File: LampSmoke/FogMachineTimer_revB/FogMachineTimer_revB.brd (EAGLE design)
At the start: 160 x 100 mm, 5 parts, among them IC1 ATTINY85-20SU, J1 M20-9980346, J2 CUI_PJ-037ACUI_PJ-037A_0_0, U1 LH1540AABTR

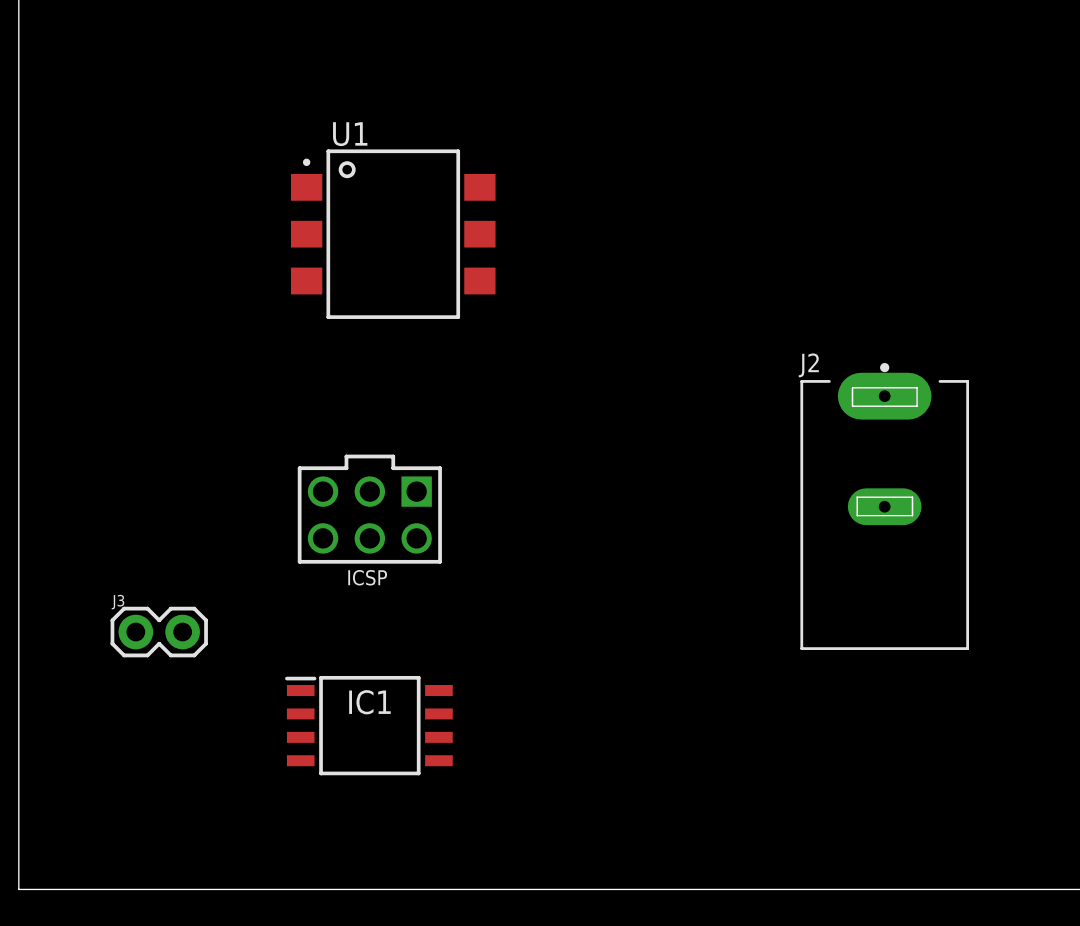
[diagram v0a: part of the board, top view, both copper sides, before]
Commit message: corrected polarity
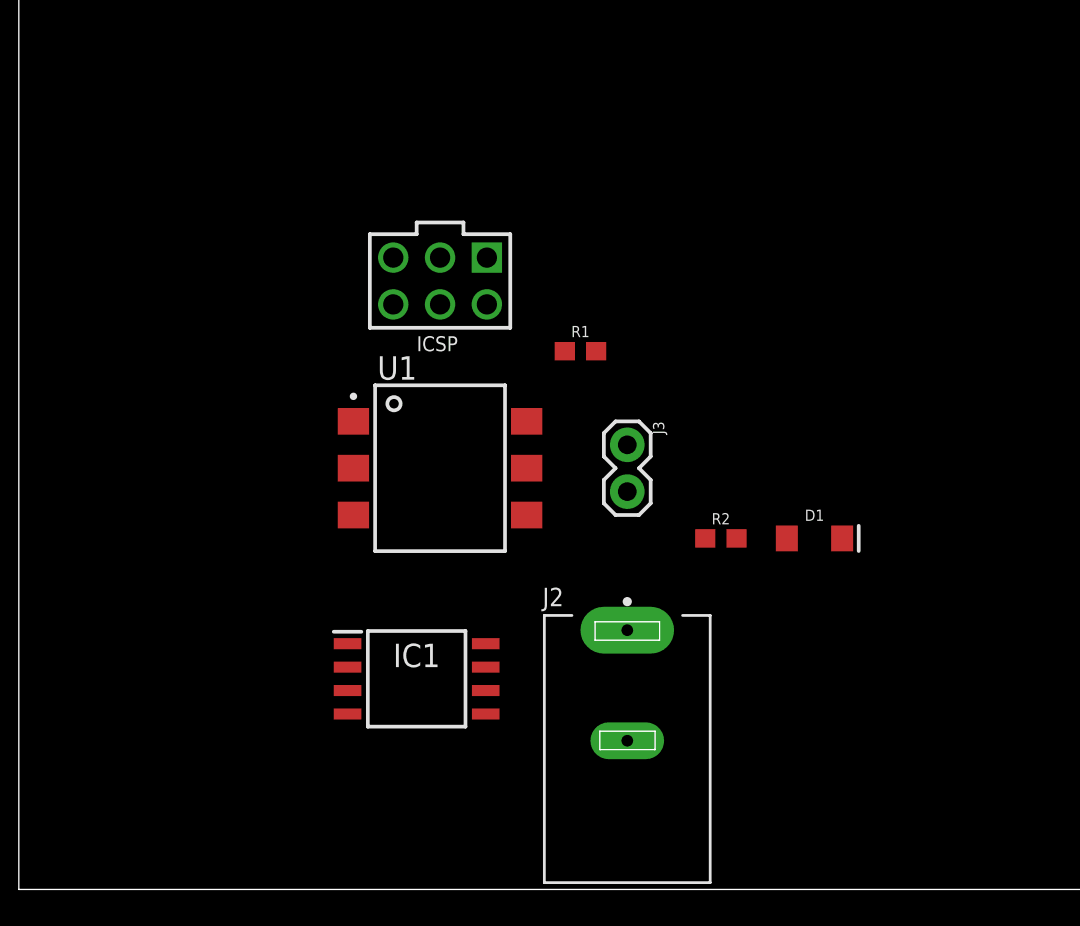
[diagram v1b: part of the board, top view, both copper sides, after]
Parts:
- added D1: (no value), SparkFun-LED:LED-1206
- added R1: 1k, SparkFun-Resistors:0603
- added R2: 220R, SparkFun-Resistors:0603
- moved J3 28.5 mm to (33.0, 24.1), turned to 270 degrees
- moved J2 18.9 mm to (33.0, 7.62)
- moved J1 13.3 mm to (22.9, 30.5)
- moved U1 13.0 mm to (22.9, 22.9)
- moved IC1 3.59 mm to (21.6, 11.4)
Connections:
- new net N$1: D1.A, R2.1
- new net U1_P6: R1.1, U1.6
- net GND: now also D1.C, U1.2; no longer U1.1
- net PB0: now also U1.1; no longer U1.2
- net PB1: now also R2.2
- net SW_POS: now also R1.2; no longer U1.6

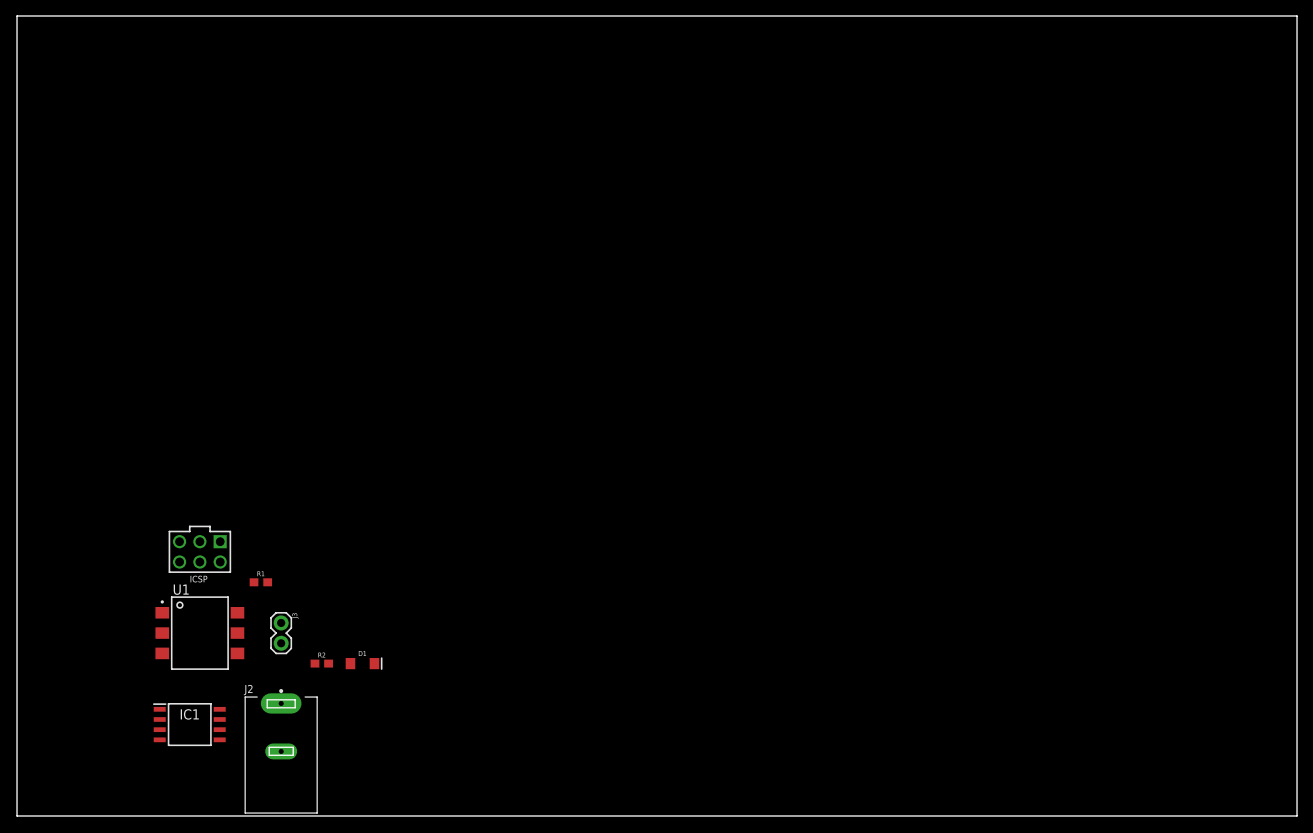
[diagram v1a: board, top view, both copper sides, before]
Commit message: FogMachineTimer revB submitted to OSHPark
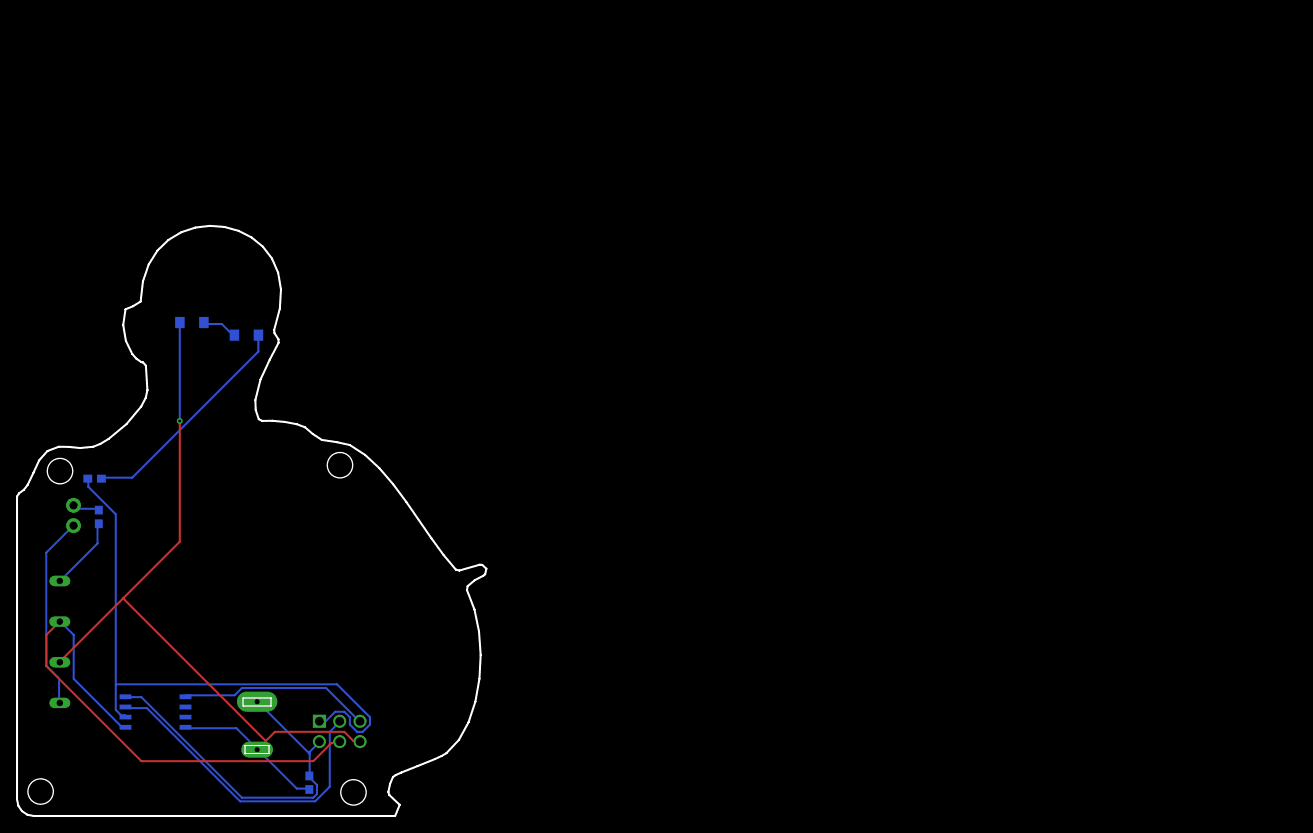
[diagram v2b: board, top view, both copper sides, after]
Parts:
- removed IC1: ATTINY85-20SU, NickParts:SOT127P798X216-8N
- removed U1: LH1540AABTR, NickParts:SOIC254P1005X390-6N
- added ATTINY85: ATTINY85-20SU, NickParts:SOT127P798X216-8N
- added C1: 0.1uF, SparkFun-Capacitors:0603
- added D2: (no value), SparkFun-LED:LED-1206
- added RELAY: HE3621A0510, NickParts:HE3621A0510
- added U$1: (no value), NickParts:5VDC_JACK_SILK
- added U$2: (no value), NickParts:DB_LOGO_MAIDEN
- R2: value 220R -> 56R
- moved D1 47.7 mm to (21.9, 61.7), flipped to the bottom
- moved R2 36.6 mm to (9.70, 42.2), flipped to the bottom
- moved J3 29.8 mm to (7.06, 38.8), flipped to the bottom
- moved J1 28.5 mm to (40.3, 8.03), flipped to the bottom
- moved R1 21.8 mm to (10.2, 37.4), flipped to the bottom, turned to 90 degrees
- moved J2 3.02 mm to (30.0, 7.84), flipped to the bottom
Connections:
- new net N$2: D2.A, R2.1
- net GND: now also ATTINY85.4, C1.1, J2.2, RELAY.2; no longer IC1.4, J2.1, U1.2
- net N$1: now also D2.C; no longer R2.1
- net PB0: now also ATTINY85.5, RELAY.3; no longer IC1.5, U1.1
- net PB1: now also ATTINY85.6; no longer IC1.6
- net PB2: now also ATTINY85.7; no longer IC1.7
- net PB3: now also ATTINY85.2; no longer IC1.2
- net PB4: now also ATTINY85.3; no longer IC1.3
- net PB5: now also ATTINY85.1; no longer IC1.1
- net SW_NEG: now also RELAY.1; no longer U1.5
- net U1_P6: now also RELAY.4; no longer U1.6
- net VCC: now also ATTINY85.8, C1.2, J2.1; no longer IC1.8, J2.2
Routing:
- net GND: track 0.00 -> 106.9 mm, vias 0 -> 1
- net PB1: track 0.00 -> 75.2 mm
- net PB0: track 0.00 -> 65.8 mm
- net VCC: track 0.00 -> 46.0 mm
- net PB2: track 0.00 -> 39.9 mm
- net N$2: track 0.00 -> 28.2 mm
- net SW_NEG: track 0.00 -> 24.3 mm
- net PB5: track 0.00 -> 24.0 mm
- net U1_P6: track 0.00 -> 9.18 mm
- net N$1: track 0.00 -> 4.46 mm
- net SW_POS: track 0.00 -> 3.51 mm
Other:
- board size 160 x 100 mm -> 58.7 x 73.8 mm
- board text added: "2019"
- board text added: "5VDC"
- board text added: "SW1 SW2"
- board text added: "smoke breath rev b © bontrager/fung"
- board text added: "“Drone Beuys” is a collaborative, non-gender specific gesture at the extension of technology as a contemporary reference to the conceptual artist Joseph Beuys, and fashioning of myth in our shared practice."

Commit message: added code and power reg
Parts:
- added C2: 0.33uF, SparkFun-Capacitors:0603
- added LM7805: 7805DT, adafruit:TO252
- R1: value 1k -> 1k5
- R2: value 56R -> 1k5
- moved R1 14.3 mm to (10.3, 23.0)
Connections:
- removed net U1_P6: R1.1, RELAY.4
- new net N$3: R1.2, RELAY.3
- new net VIN: C2.2, J2.1, LM7805.1
- net GND: now also C2.1, LM7805.3
- net PB0: now also R1.1; no longer RELAY.3
- net SW_POS: now also RELAY.4; no longer R1.2
- net VCC: now also LM7805.2; no longer J2.1
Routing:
- net GND: track 106.9 -> 145.4 mm, vias 1 -> 2
- net VIN: track 0.00 -> 17.7 mm
- net PB0: track 65.8 -> 48.3 mm
- net PB1: track 75.2 -> 64.2 mm, vias 0 -> 1
- net U1_P6: track 9.18 -> 0.00 mm
- net VCC: track 46.0 -> 37.8 mm, vias 0 -> 1
- net SW_POS: track 3.51 -> 10.2 mm
- net N$3: track 0.00 -> 5.16 mm
- net PB2: track 39.9 -> 38.3 mm
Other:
- board text added: "7-15VDC"
- board text removed: "5VDC"
